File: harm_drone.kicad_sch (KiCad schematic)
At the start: 1 part, among them IC2 Microcontroller

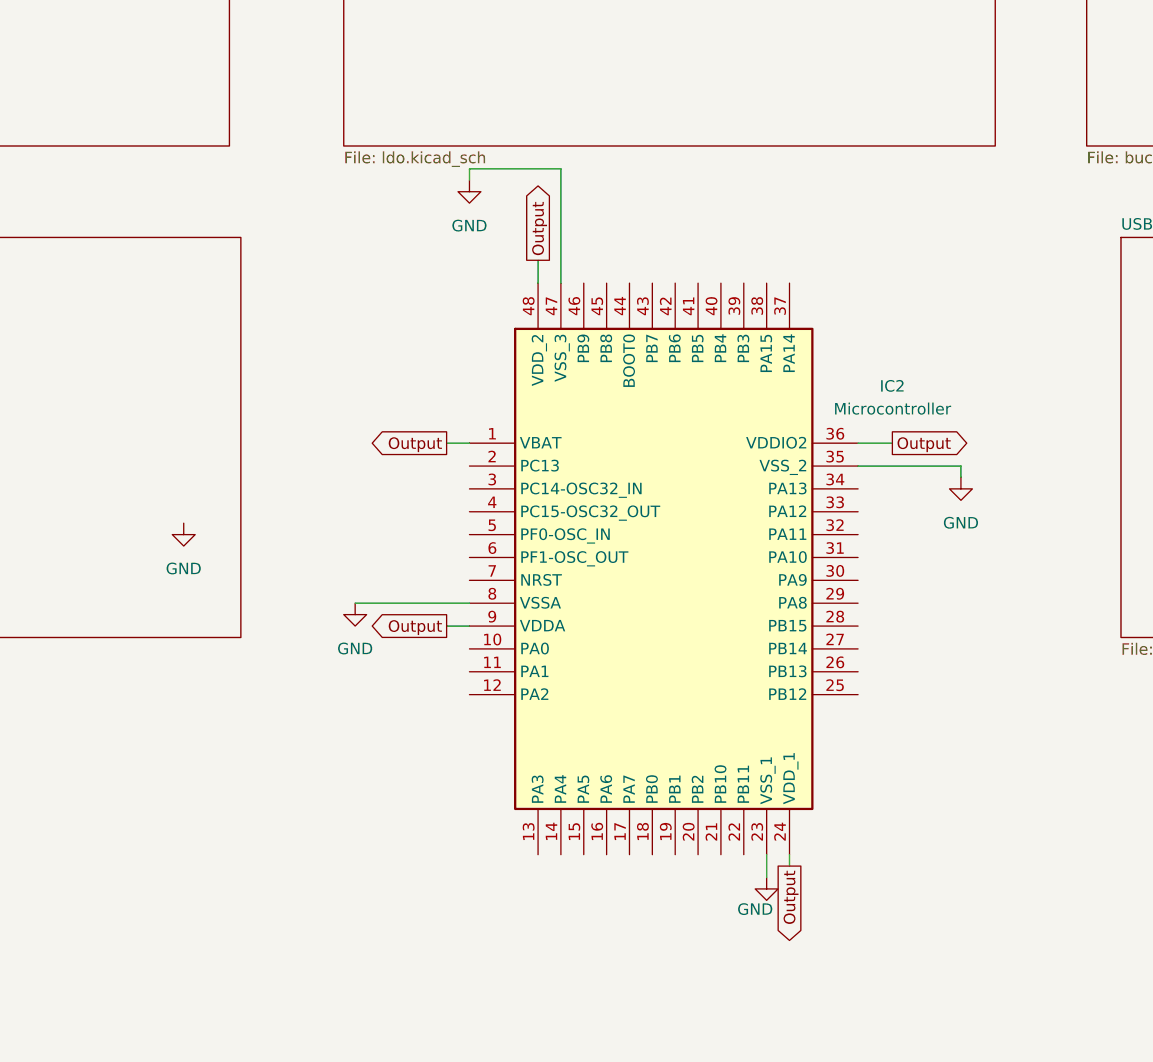
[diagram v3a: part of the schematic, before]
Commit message: Updated SPI/Microcontroller
Updated SPI schematic and connected to microcontroller
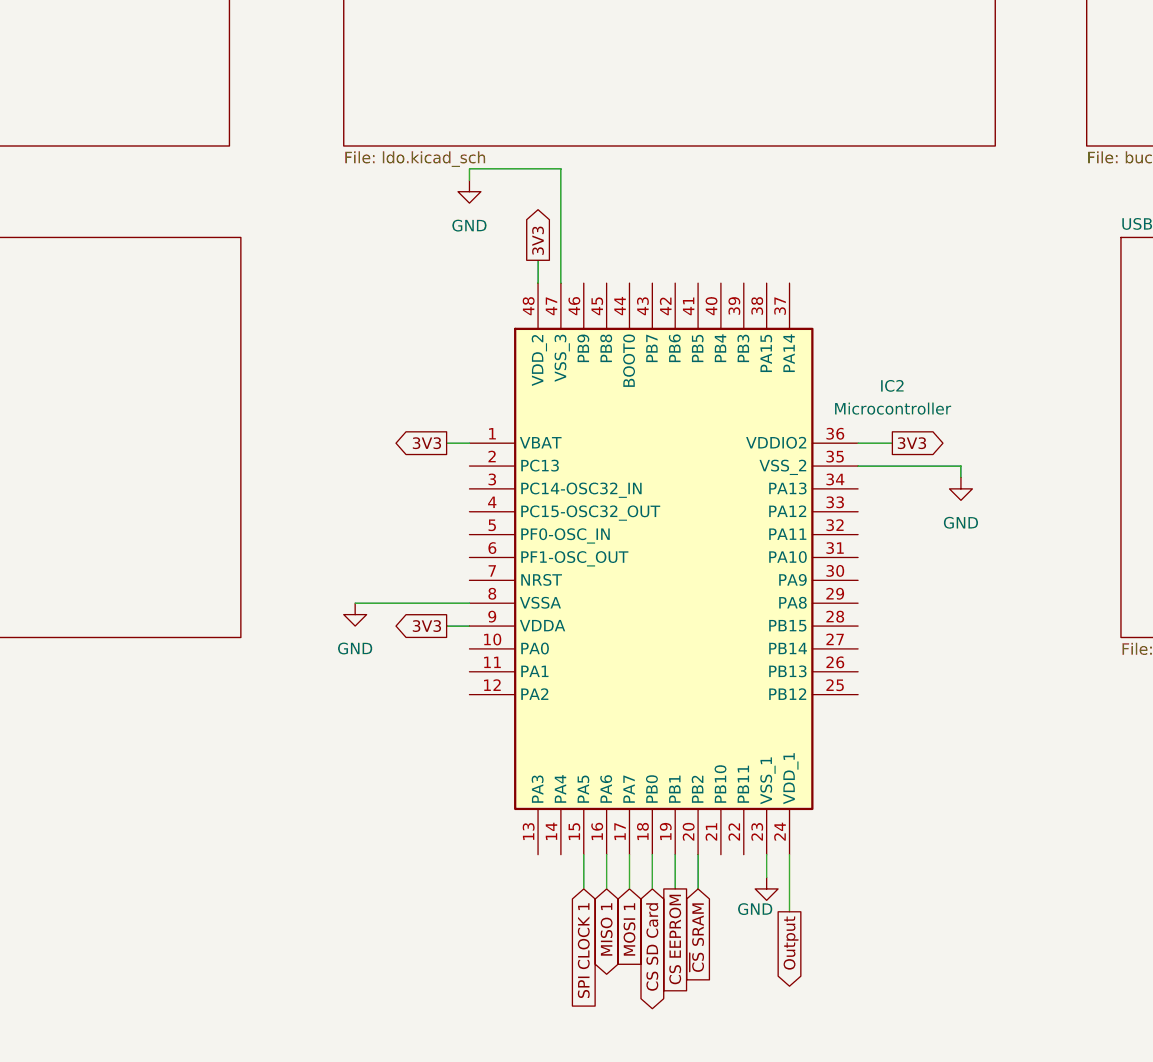
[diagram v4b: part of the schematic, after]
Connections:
- net Output: no longer IC2.1 (VBAT), IC2.36 (VDDIO2), IC2.48 (VDD_2), IC2.9 (VDDA)
- net SPI CLOCK 1: now reaches IC2.15 (PA5)
- net MISO 1: now reaches IC2.16 (PA6)
- net MOSI 1: now reaches IC2.17 (PA7)
- net CS SD Card: now reaches IC2.18 (PB0)
- net CS EEPROM: now reaches IC2.19 (PB1)
- net ~{CS} SRAM: now reaches IC2.20 (PB2)
- new net 3V3: IC2.1 (VBAT), IC2.36 (VDDIO2), IC2.48 (VDD_2), IC2.9 (VDDA)
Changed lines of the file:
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@@
+	(wire
+		(pts
+			(xy 130.81 143.51) (xy 130.81 147.32)
+		)
+		(stroke
+			(width 0)
+			(type default)
+		)
+	)
 	(wire
 		(pts
@@
 	(wire
 		(pts
+			(xy 138.43 143.51) (xy 138.43 147.32)
+		)
+		(stroke
+			(width 0)
+			(type default)
+		)
+	)
+	(wire
+		(pts
 			(xy 115.57 97.79) (xy 118.11 97.79)
 		)
@@
 	(wire
 		(pts
+			(xy 133.35 143.51) (xy 133.35 147.32)
+		)
+		(stroke
+			(width 0)
+			(type default)
+		)
+	)
+	(wire
+		(pts
 			(xy 128.27 67.31) (xy 118.11 67.31)
 		)
@@
 	(wire
 		(pts
-			(xy 153.67 143.51) (xy 153.67 144.78)
+			(xy 153.67 143.51) (xy 153.67 149.86)
 		)
 		(stroke
@@
 	(wire
 		(pts
+			(xy 135.89 143.51) (xy 135.89 147.32)
+		)
+		(stroke
+			(width 0)
+			(type default)
+		)
+	)
+	(wire
+		(pts
 			(xy 172.72 100.33) (xy 161.29 100.33)
 		)
@@
 	(wire
 		(pts
+			(xy 143.51 143.51) (xy 143.51 147.32)
+		)
+		(stroke
+			(width 0)
+			(type default)
+		)
+	)
+	(wire
+		(pts
 			(xy 151.13 143.51) (xy 151.13 146.05)
 		)
@@
 	(wire
 		(pts
+			(xy 140.97 143.51) (xy 140.97 147.32)
+		)
+		(stroke
+			(width 0)
+			(type default)
+		)
+	)
+	(wire
+		(pts
 			(xy 172.72 101.6) (xy 172.72 100.33)
 		)
@@
 			(width 0)
 			(type default)
+		)
+	)
+	(global_label "3V3"
+		(shape output)
+		(at 125.73 77.47 90)
+		(fields_autoplaced yes)
+		(effects
+			(font
+				(size 1.27 1.27)
+			)
+			(justify left)
+		)
+		(property "Intersheetrefs" "${INTERSHEET_REFS}"
+			(at 125.73 70.9772 90)
+			(effects
+				(font
+					(size 1.27 1.27)
+				)
+				(justify left)
+				(hide yes)
+			)
+		)
+	)
+	(global_label "3V3"
+		(shape output)
+		(at 165.1 97.79 0)
+		(fields_autoplaced yes)
+		(effects
+			(font
+				(size 1.27 1.27)
+			)
+			(justify left)
+		)
+		(property "Intersheetrefs" "${INTERSHEET_REFS}"
+			(at 171.5928 97.79 0)
+			(effects
+				(font
+					(size 1.27 1.27)
+				)
+				(justify left)
+				(hide yes)
+			)
+		)
+	)
+	(global_label "3V3"
+		(shape output)
+		(at 115.57 118.11 180)
+		(fields_autoplaced yes)
+		(effects
+			(font
+				(size 1.27 1.27)
+			)
+			(justify right)
+		)
+		(property "Intersheetrefs" "${INTERSHEET_REFS}"
+			(at 109.0772 118.11 0)
+			(effects
+				(font
+					(size 1.27 1.27)
+				)
+				(justify right)
+				(hide yes)
+			)
+		)
+	)
+	(global_label "MISO 1"
+		(shape bidirectional)
+		(at 133.35 147.32 270)
+		(effects
+			(font
+				(size 1.27 1.27)
+			)
+			(justify right)
+		)
+		(property "Intersheetrefs" "${INTERSHEET_REFS}"
+			(at 133.35 147.32 0)
+			(effects
+				(font
+					(size 1.27 1.27)
+				)
+				(hide yes)
+			)
+		)
+	)
+	(global_label "CS EEPROM"
+		(shape passive)
+		(at 140.97 147.32 270)
+		(effects
+			(font
+				(size 1.27 1.27)
+			)
+			(justify right)
+		)
+		(property "Intersheetrefs" "${INTERSHEET_REFS}"
+			(at 140.97 147.32 0)
+			(effects
+				(font
+					(size 1.27 1.27)
+				)
+				(hide yes)
+			)
+		)
+	)
+	(global_label "MOSI 1"
+		(shape input)
+		(at 135.89 147.32 270)
+		(effects
+			(font
+				(size 1.27 1.27)
+			)
+			(justify right)
+		)
+		(property "Intersheetrefs" "${INTERSHEET_REFS}"
+			(at 135.89 147.32 0)
+			(effects
+				(font
+					(size 1.27 1.27)
+				)
+				(hide yes)
+			)
+		)
+	)
+	(global_label "~{CS} SRAM"
+		(shape input)
+		(at 143.51 147.32 270)
+		(effects
+			(font
+				(size 1.27 1.27)
+			)
+			(justify right)
+		)
+		(property "Intersheetrefs" "${INTERSHEET_REFS}"
+			(at 143.51 147.32 0)
+			(effects
+				(font
+					(size 1.27 1.27)
+				)
+				(hide yes)
+			)
+		)
+	)
+	(global_label "3V3"
+		(shape output)
+		(at 115.57 97.79 180)
+		(fields_autoplaced yes)
+		(effects
+			(font
+				(size 1.27 1.27)
+			)
+			(justify right)
+		)
+		(property "Intersheetrefs" "${INTERSHEET_REFS}"
+			(at 109.0772 97.79 0)
+			(effects
+				(font
+					(size 1.27 1.27)
+				)
+				(justify right)
+				(hide yes)
+			)
+		)
+	)
+	(global_label "CS SD Card"
+		(shape bidirectional)
+		(at 138.43 147.32 270)
+		(effects
+			(font
+				(size 1.27 1.27)
+			)
+			(justify right)
+		)
+		(property "Intersheetrefs" "${INTERSHEET_REFS}"
+			(at 138.43 147.32 0)
+			(effects
+				(font
+					(size 1.27 1.27)
+				)
+				(hide yes)
+			)
+		)
+	)
+	(global_label "SPI CLOCK 1"
+		(shape input)
+		(at 130.81 147.32 270)
+		(effects
+			(font
+				(size 1.27 1.27)
+			)
+			(justify right)
+		)
+		(property "Intersheetrefs" "${INTERSHEET_REFS}"
+			(at 130.81 147.32 0)
+			(effects
+				(font
+					(size 1.27 1.27)
+				)
+				(hide yes)
+			)
 		)
 	)
 	(global_label "Output"
 		(shape output)
-		(at 125.73 77.47 90)
-		(fields_autoplaced yes)
-		(effects
-			(font
-				(size 1.27 1.27)
-			)
-			(justify left)
-		)
-		(property "Intersheetrefs" "${INTERSHEET_REFS}"
-			(at 125.73 68.2559 90)
-			(effects
-				(font
-					(size 1.27 1.27)
-				)
-				(justify left)
-				(hide yes)
-			)
-		)
-	)
-	(global_label "Output"
-		(shape output)
-		(at 165.1 97.79 0)
-		(fields_autoplaced yes)
-		(effects
-			(font
-				(size 1.27 1.27)
-			)
-			(justify left)
-		)
-		(property "Intersheetrefs" "${INTERSHEET_REFS}"
-			(at 174.3141 97.79 0)
-			(effects
-				(font
-					(size 1.27 1.27)
-				)
-				(justify left)
-				(hide yes)
-			)
-		)
-	)
-	(global_label "Output"
-		(shape output)
-		(at 115.57 118.11 180)
-		(fields_autoplaced yes)
-		(effects
-			(font
-				(size 1.27 1.27)
-			)
-			(justify right)
-		)
-		(property "Intersheetrefs" "${INTERSHEET_REFS}"
-			(at 106.3559 118.11 0)
-			(effects
-				(font
-					(size 1.27 1.27)
-				)
-				(justify right)
-				(hide yes)
-			)
-		)
-	)
-	(global_label "Output"
-		(shape output)
-		(at 115.57 97.79 180)
-		(fields_autoplaced yes)
-		(effects
-			(font
-				(size 1.27 1.27)
-			)
-			(justify right)
-		)
-		(property "Intersheetrefs" "${INTERSHEET_REFS}"
-			(at 106.3559 97.79 0)
-			(effects
-				(font
-					(size 1.27 1.27)
-				)
-				(justify right)
-				(hide yes)
-			)
-		)
-	)
-	(global_label "Output"
-		(shape output)
-		(at 153.67 144.78 270)
-		(fields_autoplaced yes)
-		(effects
-			(font
-				(size 1.27 1.27)
-			)
-			(justify right)
-		)
-		(property "Intersheetrefs" "${INTERSHEET_REFS}"
-			(at 153.67 153.9941 90)
+		(at 153.67 149.86 270)
+		(fields_autoplaced yes)
+		(effects
+			(font
+				(size 1.27 1.27)
+			)
+			(justify right)
+		)
+		(property "Intersheetrefs" "${INTERSHEET_REFS}"
+			(at 153.67 159.0741 90)
 			(effects
 				(font
@@
 					(unit 1)
 				)
-			)
-		)
-	)
-	(symbol
-		(lib_id "power:GND")
-		(at 86.36 106.68 0)
-		(unit 1)
-		(exclude_from_sim no)
-		(in_bom yes)
-		(on_board yes)
-		(dnp no)
-		(fields_autoplaced yes)
-		(property "Reference" "#PWR01"
-			(at 86.36 113.03 0)
-			(effects
-				(font
-					(size 1.27 1.27)
-				)
-				(hide yes)
-			)
-		)
-		(property "Value" "GND"
-			(at 86.36 111.76 0)
-			(effects
-				(font
-					(size 1.27 1.27)
-				)
-			)
-		)
-		(property "Footprint" ""
-			(at 86.36 106.68 0)
-			(effects
-				(font
-					(size 1.27 1.27)
-				)
-				(hide yes)
-			)
-		)
-		(property "Datasheet" ""
-			(at 86.36 106.68 0)
-			(effects
-				(font
-					(size 1.27 1.27)
-				)
-				(hide yes)
-			)
-		)
-		(property "Description" "Power symbol creates a global label with name \"GND\" , ground"
-			(at 86.36 106.68 0)
-			(effects
-				(font
-					(size 1.27 1.27)
-				)
-				(hide yes)
-			)
-		)
-		(pin "1"
-		)
-		(instances
-			(project ""
-				(path "/5ce3566e-4e0f-420e-9b0d-3952cd3c63fd"
-					(reference "#PWR01")
-					(unit 1)
-				)

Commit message: finished up schematic
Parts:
- added C1: 0805Capacitor, Capacitor_SMD:C_0805_2012Metric, symbol group127:0805Capacitor
- added J1: SYS_DEBUG, symbol Connector:Conn_01x03_Pin
- added S1: KSR221GLFS, symbol group127:KSR221GLFS
- IC1: renamed from IC2; footprint QFP50P900X900X160-48N -> (none)
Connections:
- net GND: now also IC1.44 (BOOT0), C1.1, J1.1 (Pin_1), S1.1 (COM)
- net SPI CLOCK 2: now reaches IC1.21 (PB10)
- net ~{USB_RESET}: now reaches IC1.25 (PB12)
- net SUSPND: now reaches IC1.26 (PB13)
- net MISO 2: now reaches IC1.27 (PB14)
- net MOSI 2: now reaches IC1.28 (PB15)
- net TSTPLL/48MCLK: now reaches IC1.29 (PA8)
- net RXD_USB2SERIAL: now reaches IC1.30 (PA9)
- net TXD_USB2SERIAL: now reaches IC1.31 (PA10)
- net DM0: now reaches IC1.32 (PA11)
- net DP0: now reaches IC1.33 (PA12)
- net at IC1.34 (PA13): now also J1.2 (Pin_2)
- net at IC1.37 (PA14): now also J1.3 (Pin_3)
- net at IC1.7 (NRST): now also C1.2, S1.2 (NO)

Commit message: more footprint updates
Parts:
- J1: footprint (none) -> Connector_PinHeader_2.54mm:PinHeader_1x02_P2.54mm_Vertical
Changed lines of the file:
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@@
 			)
 		)
-		(property "Footprint" ""
+		(property "Footprint" "Connector_PinHeader_2.54mm:PinHeader_1x02_P2.54mm_Vertical"
 			(at 165.1 74.93 0)
 			(effects

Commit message: initial PCB draft!
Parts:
- added C15, C18, C19, C21: 10uF, Capacitor_SMD:C_0805_2012Metric, symbol group127:0805Capacitor
- added C16, C17, C20, C22: 0.1uF, Capacitor_SMD:C_0805_2012Metric, symbol group127:0805Capacitor
- C1: value 0805Capacitor -> 0.1uF
- IC1: footprint (none) -> group127:Microcontroller
- J1: footprint Connector_PinHeader_2.54mm:PinHeader_1x02_P2.54mm_Vertical -> Connector_PinHeader_2.54mm:PinHeader_1x03_P2.54mm_Vertical
- S1: footprint (none) -> group127:Button
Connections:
- net Output is gone; now on net 3V3: IC1.24 (VDD_1)
- net 3V3: now also C15.2, C16.2, C17.2, C18.2, C19.1, C20.1, C21.1, C22.1
- net GND: now also C15.1, C16.1, C17.1, C18.1, C19.2, C20.2, C21.2, C22.2

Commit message: namespace change
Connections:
- net DM0 renamed D0-
- net DP0 renamed D0+
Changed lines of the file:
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@@
 		)
 	)
-	(global_label "DM0"
+	(global_label "D0-"
 		(shape input)
 		(at 161.29 107.95 0)
@@
 		)
 	)
-	(global_label "DP0"
+	(global_label "D0+"
 		(shape input)
 		(at 161.29 105.41 0)
